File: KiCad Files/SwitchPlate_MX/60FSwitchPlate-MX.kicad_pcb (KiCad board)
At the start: 2 copper layers, 283 x 96 mm, 9 parts

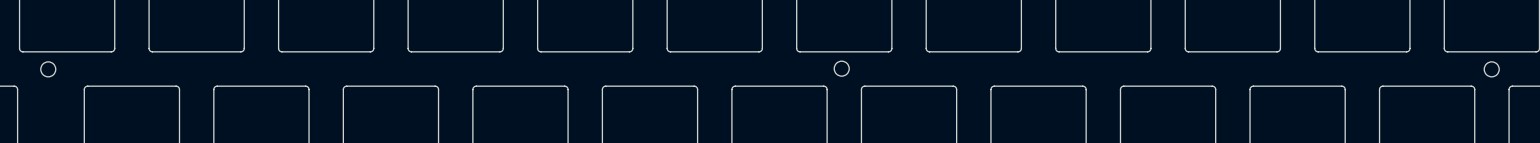
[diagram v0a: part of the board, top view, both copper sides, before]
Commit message: fixed parity between main MX PCB and switch plate.
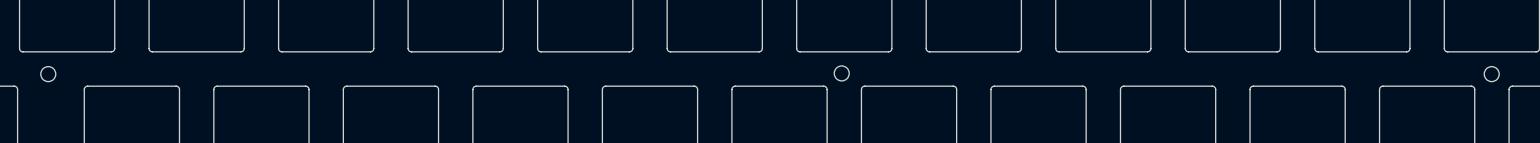
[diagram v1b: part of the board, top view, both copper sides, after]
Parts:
- moved H10 0.70 mm to (314.1, 84.8)
- moved H4 0.70 mm to (101.8, 84.8)
- moved H9 0.70 mm to (218.5, 84.7)
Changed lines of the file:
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@@
     )
     (pad_to_mask_clearance 0.051)
-    (solder_mask_min_width 0.25)
     (pcbplotparams
       (layerselection 0x00010fc_ffffffff)
@@
   )
   (footprint "Env_Extras:MountingHole_2.2mm_M2-MODIFIED" (layer "F.Cu")
-    (at 218.5 84)
+    (at 218.5 84.7)
     (descr "Mounting Hole 2.2mm, no annular, M2")
     (tags "mounting hole 2.2mm no annular m2")
@@
   )
   (footprint "Env_Extras:MountingHole_2.2mm_M2-MODIFIED" (layer "F.Cu")
-    (at 314.1 84.1)
+    (at 314.1 84.8)
     (descr "Mounting Hole 2.2mm, no annular, M2")
     (tags "mounting hole 2.2mm no annular m2")
@@
   )
   (footprint "Env_Extras:MountingHole_2.2mm_M2-MODIFIED" (layer "F.Cu")
-    (at 101.8 84.1)
+    (at 101.8 84.8)
     (descr "Mounting Hole 2.2mm, no annular, M2")
     (tags "mounting hole 2.2mm no annular m2")

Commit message: Decided extended plates are the norm.
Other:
- board size 283 x 96 mm -> 287 x 99.9 mm
